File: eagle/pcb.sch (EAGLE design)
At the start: 58 parts, among them J7 FEMALE 2x3, X1 16 MHz, X2 12 MHz

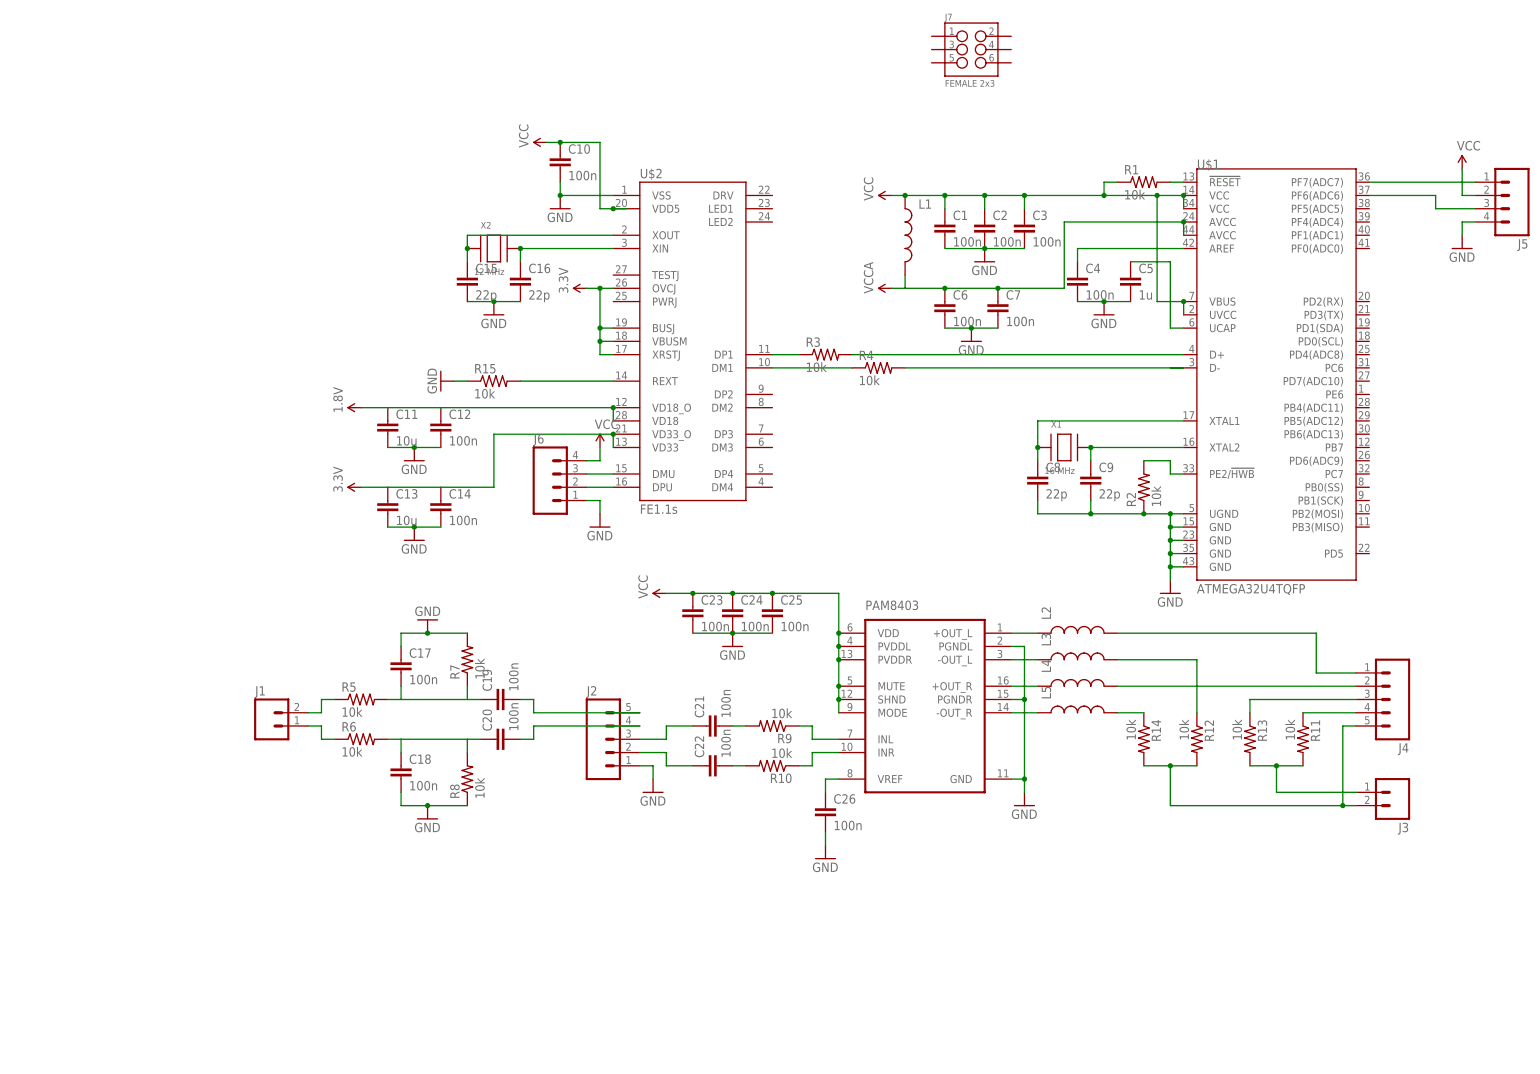
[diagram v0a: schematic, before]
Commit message: top layer almost done, continue with bottom layer
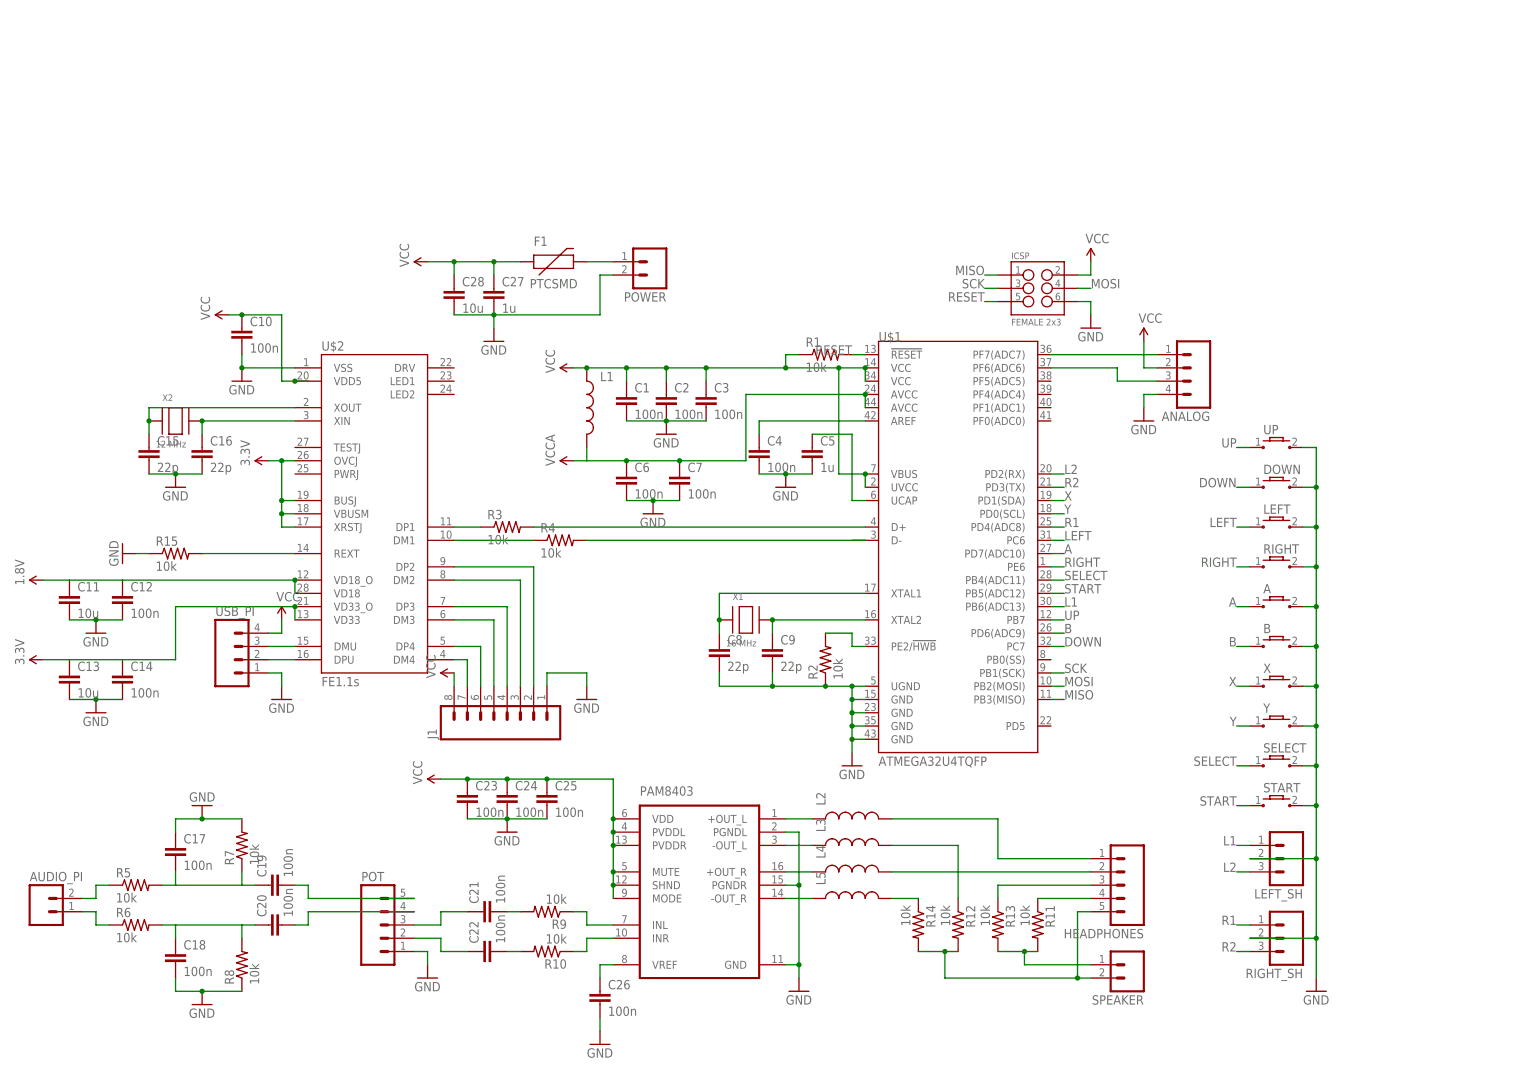
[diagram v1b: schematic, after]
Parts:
- removed J2, J4: (no value), SparkFun-Connectors:M05PTH
- removed J3: (no value), SparkFun-Connectors:M02PTH
- removed J5, J6: (no value), SparkFun-Connectors:M04PTH
- removed J7: FEMALE 2x3, SparkFun-Connectors:M03X2FEMALE
- added A, B, DOWN, LEFT, RIGHT, UP, X, Y: (no value), dmg-conductive:DMG_CONDUCTIVE
- added ANALOG, USB_PI: (no value), SparkFun-Connectors:M04PTH
- added AUDIO_PI, POWER, SPEAKER: (no value), SparkFun-Connectors:M02PTH
- added C27: 1u, SparkFun-Passives:CAP0805
- added C28: 10u, SparkFun-Passives:CAP0805
- added F1: PTCSMD, SparkFun-PowerIC:PTCSMD
- added HEADPHONES, POT: (no value), SparkFun-Connectors:M05PTH
- added ICSP: FEMALE 2x3, SparkFun-Connectors:M03X2FEMALE
- added LEFT_SH, RIGHT_SH: (no value), SparkFun-Connectors:M03PTH
- added SELECT, START: (no value), dmg-conductive:DMG_CONDUCTIVE2
- J1: device SparkFun-Connectors:M02PTH -> SparkFun-Connectors:M08
- X1, X2: device adafruit:XTALNX8045 -> adafruit:XTALNX5032
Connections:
- removed net N$1: R1.2, U$1.!RESET
- removed net N$27: J4.1, L2.2
- removed net N$31: J4.2, L4.2
- removed net N$38: J3.1, R11.2, R13.2
- new net A: A.1, U$1.PD7(ADC10)
- new net AUDIO_GND: HEADPHONES.5, R12.2, R14.2, SPEAKER.2
- new net AUDIO_L2MONO: HEADPHONES.4, R11.1
- new net AUDIO_MONO: R11.2, R13.2, SPEAKER.1
- new net AUDIO_R2MONO: HEADPHONES.3, R13.1
- new net AUDIO_STEREO_L: HEADPHONES.1, L2.2
- new net AUDIO_STEREO_R: HEADPHONES.2, L4.2
- new net B: B.1, U$1.PD6(ADC9)
- new net DOWN: DOWN.1, U$1.PC7
- new net L1: LEFT_SH.1, U$1.PB6(ADC13)
- new net L2: LEFT_SH.3, U$1.PD2(RX)
- new net LEFT: LEFT.1, U$1.PC6
- new net MISO: ICSP.1, U$1.PB3(MISO)
- new net MOSI: ICSP.4, U$1.PB2(MOSI)
- new net N$34: J1.7, U$2.DM4
- new net N$40: J1.3, U$2.DM2
- new net N$43: J1.2, U$2.DP2
- new net N$50: F1.2, POWER.1
- new net R1: RIGHT_SH.1, U$1.PD4(ADC8)
- new net R2: RIGHT_SH.3, U$1.PD3(TX)
- new net RESET: ICSP.5, R1.2, U$1.!RESET
- new net RIGHT: RIGHT.1, U$1.PE6
- new net SCK: ICSP.3, U$1.PB1(SCK)
- new net SELECT: SELECT.1, U$1.PB4(ADC11)
- new net START: START.1, U$1.PB5(ADC12)
- new net UP: U$1.PB7, UP.1
- new net X: U$1.PD1(SDA), X.1
- new net Y: U$1.PD0(SCL), Y.1
- net GND: now also A.2, ANALOG.4, B.2, C27.2, C28.2, DOWN.2, ICSP.6, J1.1, LEFT.2, LEFT_SH.2, POT.1, POWER.2, RIGHT.2, RIGHT_SH.2, SELECT.2, START.2, UP.2, USB_PI.1, X.2, Y.2; no longer J2.1, J5.4, J6.1
- net N$13: now also AUDIO_PI.2; no longer J1.2
- net N$14: now also AUDIO_PI.1; no longer J1.1
- net N$19: now also POT.5; no longer J2.5
- net N$20: now also POT.4; no longer J2.4
- net N$21: now also POT.3; no longer J2.3
- net N$22: now also POT.2; no longer J2.2
- net N$35: now also J1.6, U$2.DP4; no longer J4.3, R13.1
- net N$36: now also J1.5, U$2.DM3; no longer J4.4, R11.1
- net N$39: now also J1.4, U$2.DP3; no longer J3.2, J4.5, R12.2, R14.2
- net N$41: now also ANALOG.1; no longer J5.1
- net N$42: now also ANALOG.3; no longer J5.3
- net N$45: now also USB_PI.3; no longer J6.3
- net N$46: now also USB_PI.2; no longer J6.2
- net VCC: now also ANALOG.2, C27.1, C28.1, F1.1, ICSP.2, J1.8, USB_PI.4; no longer J5.2, J6.4
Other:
- moved on the sheet: C1, C10, C11, C12, C13, C14, C15, C16, C17, C18, C19, C2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

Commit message: completed routing top and bottom
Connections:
- removed net N$50: F1.2, POWER.1
- new net VCC_POWER: F1.2, POWER.1, USB_PI.4
- net VCC: no longer USB_PI.4
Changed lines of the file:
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@@
 <part name="USB_PI" library="SparkFun-Connectors" deviceset="M04" device="PTH"/>
 <part name="GND17" library="SparkFun-Aesthetics" deviceset="GND" device=""/>
-<part name="SUPPLY8" library="SparkFun-Aesthetics" deviceset="VCC" device=""/>
 <part name="ICSP" library="SparkFun-Connectors" deviceset="M03X2" device="FEMALE" value="FEMALE 2x3"/>
 <part name="GND18" library="SparkFun-Aesthetics" deviceset="GND" device=""/>
@@
 <instance part="USB_PI" gate="G$1" x="48.26" y="91.44"/>
 <instance part="GND17" gate="1" x="55.88" y="83.82"/>
-<instance part="SUPPLY8" gate="G$1" x="55.88" y="99.06"/>
 <instance part="ICSP" gate="G$1" x="200.66" y="162.56"/>
 <instance part="GND18" gate="1" x="210.82" y="154.94"/>
@@
 <wire x1="220.98" y1="147.32" x2="220.98" y2="152.4" width="0.1524" layer="91"/>
 <pinref part="SUPPLY7" gate="G$1" pin="VCC"/>
-</segment>
-<segment>
-<pinref part="USB_PI" gate="G$1" pin="4"/>
-<wire x1="53.34" y1="96.52" x2="55.88" y2="96.52" width="0.1524" layer="91"/>
-<wire x1="55.88" y1="96.52" x2="55.88" y2="99.06" width="0.1524" layer="91"/>
-<pinref part="SUPPLY8" gate="G$1" pin="VCC"/>
 </segment>
 <segment>
@@
 </segment>
 </net>
-<net name="N$50" class="0">
+<net name="VCC_POWER" class="0">
 <segment>
 <pinref part="F1" gate="G$1" pin="2"/>
 <pinref part="POWER" gate="G$1" pin="1"/>
 <wire x1="114.3" y1="167.64" x2="119.38" y2="167.64" width="0.1524" layer="91"/>
-</segment>
-</net>
+<label x="114.3" y="167.64" size="1.778" layer="95"/>
+</segment>
+<segment>
+<pinref part="USB_PI" gate="G$1" pin="4"/>
+<wire x1="53.34" y1="96.52" x2="55.88" y2="96.52" width="0.1524" layer="91"/>
+<label x="55.88" y="96.52" size="1.778" layer="95"/>
+</segment>
+</net>

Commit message: finished v0.2 and gerber files
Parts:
- C17, C18: value 100n -> 33n
- C19, C20: value 100n -> 10u
- C21, C22: value 100n -> 220n
- C26: value 100n -> 1u
- R11, R12, R13, R14: value 10k -> 100
- R15: value 10k -> 2.7k
- R3, R4: value 10k -> 22
- R5, R6: value 10k -> 270
- R7, R8: value 10k -> 150
- renumbered J1 to USB_HUB
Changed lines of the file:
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@@
 <part name="GND4" library="SparkFun-Aesthetics" deviceset="GND" device=""/>
 <part name="R2" library="SparkFun-Passives" deviceset="RESISTOR" device="0805-RES" value="10k"/>
-<part name="R3" library="SparkFun-Passives" deviceset="RESISTOR" device="0805-RES" value="10k"/>
-<part name="R4" library="SparkFun-Passives" deviceset="RESISTOR" device="0805-RES" value="10k"/>
+<part name="R3" library="SparkFun-Passives" deviceset="RESISTOR" device="0805-RES" value="22"/>
+<part name="R4" library="SparkFun-Passives" deviceset="RESISTOR" device="0805-RES" value="22"/>
 <part name="C10" library="SparkFun-Passives" deviceset="CAP" device="0805" value="100n"/>
 <part name="C11" library="SparkFun-Passives" deviceset="CAP" device="0805" value="10u"/>
@@
 <part name="SUPPLY4" library="SparkFun-Aesthetics" deviceset="1.8V" device=""/>
 <part name="AUDIO_PI" library="SparkFun-Connectors" deviceset="M02" device="PTH"/>
-<part name="R5" library="SparkFun-Passives" deviceset="RESISTOR" device="0805-RES" value="10k"/>
-<part name="R6" library="SparkFun-Passives" deviceset="RESISTOR" device="0805-RES" value="10k"/>
-<part name="C17" library="SparkFun-Passives" deviceset="CAP" device="0805" value="100n"/>
-<part name="C18" library="SparkFun-Passives" deviceset="CAP" device="0805" value="100n"/>
-<part name="R7" library="SparkFun-Passives" deviceset="RESISTOR" device="0805-RES" value="10k"/>
-<part name="R8" library="SparkFun-Passives" deviceset="RESISTOR" device="0805-RES" value="10k"/>
-<part name="C19" library="SparkFun-Passives" deviceset="CAP" device="0805" value="100n"/>
-<part name="C20" library="SparkFun-Passives" deviceset="CAP" device="0805" value="100n"/>
+<part name="R5" library="SparkFun-Passives" deviceset="RESISTOR" device="0805-RES" value="270"/>
+<part name="R6" library="SparkFun-Passives" deviceset="RESISTOR" device="0805-RES" value="270"/>
+<part name="C17" library="SparkFun-Passives" deviceset="CAP" device="0805" value="33n"/>
+<part name="C18" library="SparkFun-Passives" deviceset="CAP" device="0805" value="33n"/>
+<part name="R7" library="SparkFun-Passives" deviceset="RESISTOR" device="0805-RES" value="150"/>
+<part name="R8" library="SparkFun-Passives" deviceset="RESISTOR" device="0805-RES" value="150"/>
+<part name="C19" library="SparkFun-Passives" deviceset="CAP" device="0805" value="10u"/>
+<part name="C20" library="SparkFun-Passives" deviceset="CAP" device="0805" value="10u"/>
 <part name="POT" library="SparkFun-Connectors" deviceset="M05" device="PTH"/>
-<part name="C21" library="SparkFun-Passives" deviceset="CAP" device="0805" value="100n"/>
-<part name="C22" library="SparkFun-Passives" deviceset="CAP" device="0805" value="100n"/>
+<part name="C21" library="SparkFun-Passives" deviceset="CAP" device="0805" value="220n"/>
+<part name="C22" library="SparkFun-Passives" deviceset="CAP" device="0805" value="220n"/>
 <part name="R9" library="SparkFun-Passives" deviceset="RESISTOR" device="0805-RES" value="10k"/>
 <part name="R10" library="SparkFun-Passives" deviceset="RESISTOR" device="0805-RES" value="10k"/>
@@
 <part name="GND11" library="SparkFun-Aesthetics" deviceset="GND" device=""/>
 <part name="GND12" library="SparkFun-Aesthetics" deviceset="GND" device=""/>
-<part name="C26" library="SparkFun-Passives" deviceset="CAP" device="0805" value="100n"/>
+<part name="C26" library="SparkFun-Passives" deviceset="CAP" device="0805" value="1u"/>
 <part name="GND13" library="SparkFun-Aesthetics" deviceset="GND" device=""/>
 <part name="GND14" library="SparkFun-Aesthetics" deviceset="GND" device=""/>
@@
 <part name="L4" library="SparkFun-Passives" deviceset="INDUCTOR" device="0805"/>
 <part name="L5" library="SparkFun-Passives" deviceset="INDUCTOR" device="0805"/>
-<part name="R11" library="SparkFun-Passives" deviceset="RESISTOR" device="0805-RES" value="10k"/>
-<part name="R12" library="SparkFun-Passives" deviceset="RESISTOR" device="0805-RES" value="10k"/>
-<part name="R13" library="SparkFun-Passives" deviceset="RESISTOR" device="0805-RES" value="10k"/>
-<part name="R14" library="SparkFun-Passives" deviceset="RESISTOR" device="0805-RES" value="10k"/>
+<part name="R11" library="SparkFun-Passives" deviceset="RESISTOR" device="0805-RES" value="100"/>
+<part name="R12" library="SparkFun-Passives" deviceset="RESISTOR" device="0805-RES" value="100"/>
+<part name="R13" library="SparkFun-Passives" deviceset="RESISTOR" device="0805-RES" value="100"/>
+<part name="R14" library="SparkFun-Passives" deviceset="RESISTOR" device="0805-RES" value="100"/>
 <part name="SPEAKER" library="SparkFun-Connectors" deviceset="M02" device="PTH"/>
-<part name="R15" library="SparkFun-Passives" deviceset="RESISTOR" device="0805-RES" value="10k"/>
+<part name="R15" library="SparkFun-Passives" deviceset="RESISTOR" device="0805-RES" value="2.7k"/>
 <part name="GND15" library="SparkFun-Aesthetics" deviceset="GND" device=""/>
 <part name="SUPPLY6" library="SparkFun-Aesthetics" deviceset="3.3V" device=""/>
@@
 <part name="SUPPLY11" library="SparkFun-Aesthetics" deviceset="VCC" device=""/>
 <part name="FRAME2" library="frames" deviceset="A4L-LOC" device=""/>
-<part name="J1" library="SparkFun-Connectors" deviceset="M08" device=""/>
+<part name="USB_HUB" library="SparkFun-Connectors" deviceset="M08" device=""/>
 <part name="C28" library="SparkFun-Passives" deviceset="CAP" device="0805" value="10u"/>
 </parts>
@@
 <instance part="SUPPLY11" gate="G$1" x="83.82" y="167.64" rot="R90"/>
 <instance part="FRAME2" gate="G$1" x="0" y="0"/>
-<instance part="J1" gate="G$1" x="99.06" y="81.28" rot="R90"/>
+<instance part="USB_HUB" gate="G$1" x="99.06" y="81.28" rot="R90"/>
 <instance part="C28" gate="G$1" x="88.9" y="160.02"/>
 </instances>
@@
 <segment>
 <pinref part="SUPPLY10" gate="G$1" pin="VCC"/>
-<pinref part="J1" gate="G$1" pin="8"/>
+<pinref part="USB_HUB" gate="G$1" pin="8"/>
 <wire x1="88.9" y1="88.9" x2="88.9" y2="86.36" width="0.1524" layer="91"/>
 </segment>
@@
 <wire x1="114.3" y1="88.9" x2="114.3" y2="86.36" width="0.1524" layer="91"/>
 <pinref part="GND20" gate="1" pin="GND"/>
-<pinref part="J1" gate="G$1" pin="1"/>
+<pinref part="USB_HUB" gate="G$1" pin="1"/>
 <wire x1="114.3" y1="88.9" x2="106.68" y2="88.9" width="0.1524" layer="91"/>
 <wire x1="106.68" y1="88.9" x2="106.68" y2="86.36" width="0.1524" layer="91"/>
@@
 <segment>
 <pinref part="U$2" gate="G$1" pin="DM4"/>
-<pinref part="J1" gate="G$1" pin="7"/>
+<pinref part="USB_HUB" gate="G$1" pin="7"/>
 <wire x1="88.9" y1="91.44" x2="91.44" y2="91.44" width="0.1524" layer="91"/>
 <wire x1="91.44" y1="91.44" x2="91.44" y2="86.36" width="0.1524" layer="91"/>
@@
 <segment>
 <pinref part="U$2" gate="G$1" pin="DP4"/>
-<pinref part="J1" gate="G$1" pin="6"/>
+<pinref part="USB_HUB" gate="G$1" pin="6"/>
 <wire x1="88.9" y1="93.98" x2="93.98" y2="93.98" width="0.1524" layer="91"/>
 <wire x1="93.98" y1="93.98" x2="93.98" y2="86.36" width="0.1524" layer="91"/>
@@
 <segment>
 <pinref part="U$2" gate="G$1" pin="DM3"/>
-<pinref part="J1" gate="G$1" pin="5"/>
+<pinref part="USB_HUB" gate="G$1" pin="5"/>
 <wire x1="88.9" y1="99.06" x2="96.52" y2="99.06" width="0.1524" layer="91"/>
 <wire x1="96.52" y1="99.06" x2="96.52" y2="86.36" width="0.1524" layer="91"/>
@@
 <segment>
 <pinref part="U$2" gate="G$1" pin="DP3"/>
-<pinref part="J1" gate="G$1" pin="4"/>
+<pinref part="USB_HUB" gate="G$1" pin="4"/>
 <wire x1="88.9" y1="101.6" x2="99.06" y2="101.6" width="0.1524" layer="91"/>
 <wire x1="99.06" y1="101.6" x2="99.06" y2="86.36" width="0.1524" layer="91"/>
@@
 <wire x1="88.9" y1="106.68" x2="101.6" y2="106.68" width="0.1524" layer="91"/>
 <wire x1="101.6" y1="106.68" x2="101.6" y2="86.36" width="0.1524" layer="91"/>
-<pinref part="J1" gate="G$1" pin="3"/>
+<pinref part="USB_HUB" gate="G$1" pin="3"/>
 </segment>
 </net>
@@
 <segment>
 <pinref part="U$2" gate="G$1" pin="DP2"/>
-<pinref part="J1" gate="G$1" pin="2"/>
+<pinref part="USB_HUB" gate="G$1" pin="2"/>
 <wire x1="88.9" y1="109.22" x2="104.14" y2="109.22" width="0.1524" layer="91"/>
 <wire x1="104.14" y1="109.22" x2="104.14" y2="86.36" width="0.1524" layer="91"/>
